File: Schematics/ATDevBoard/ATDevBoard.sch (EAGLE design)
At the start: 42 parts, among them U1 TINY85-20-DIP

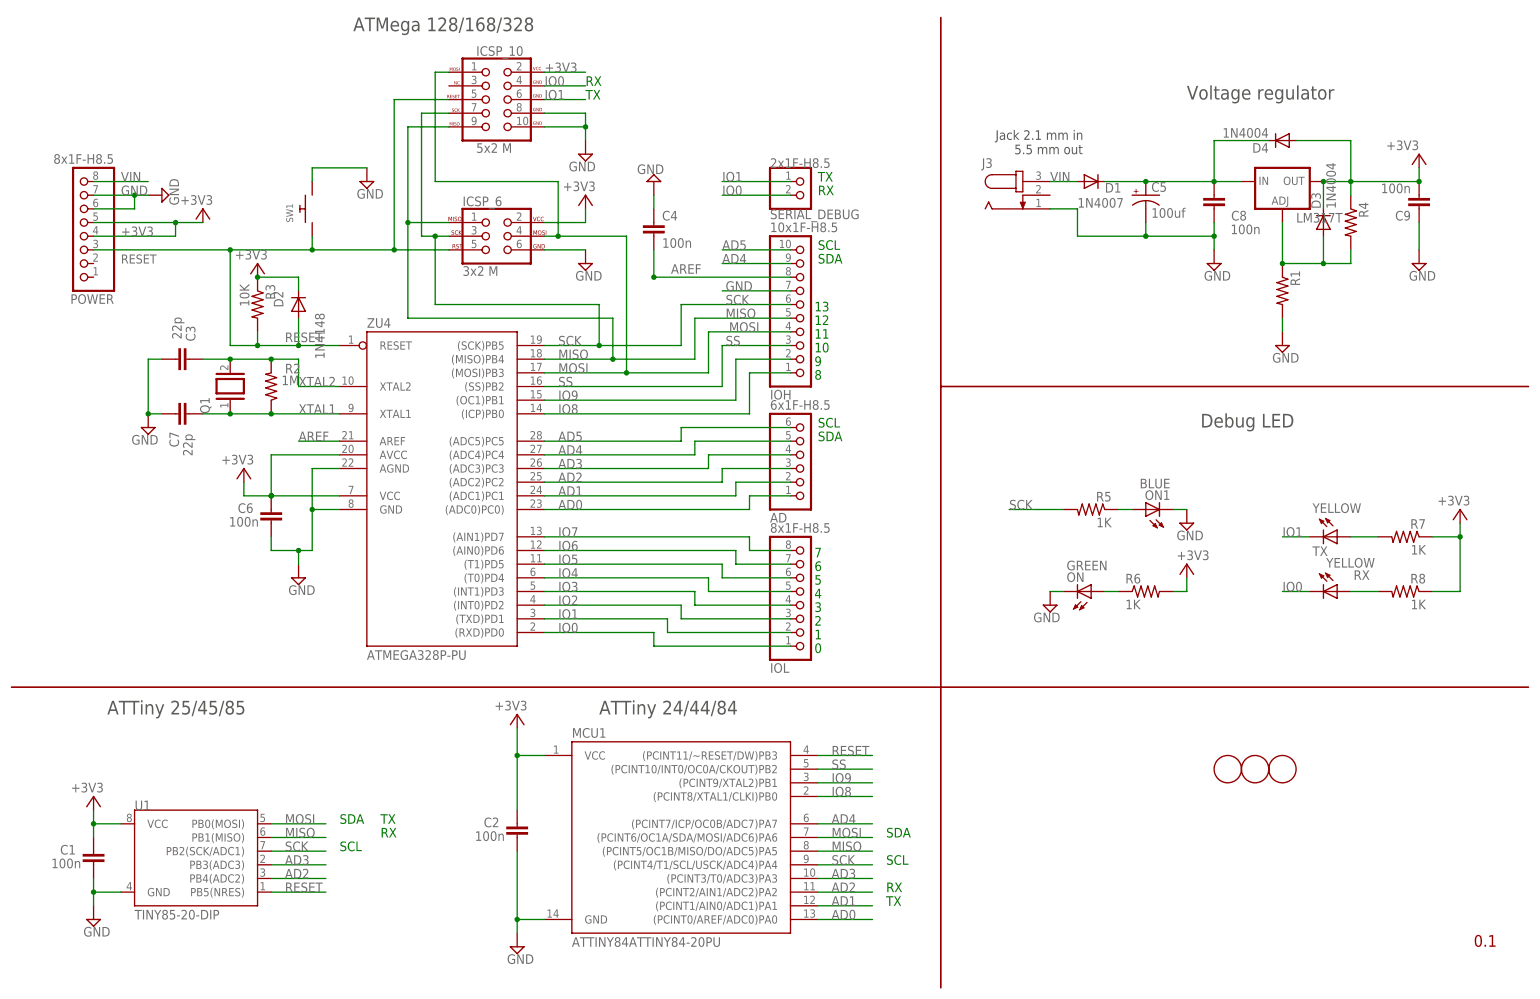
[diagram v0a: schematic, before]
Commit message: Added vaule for regulator resistors, first routed version of brd. Added pdfs for brd and schematic.
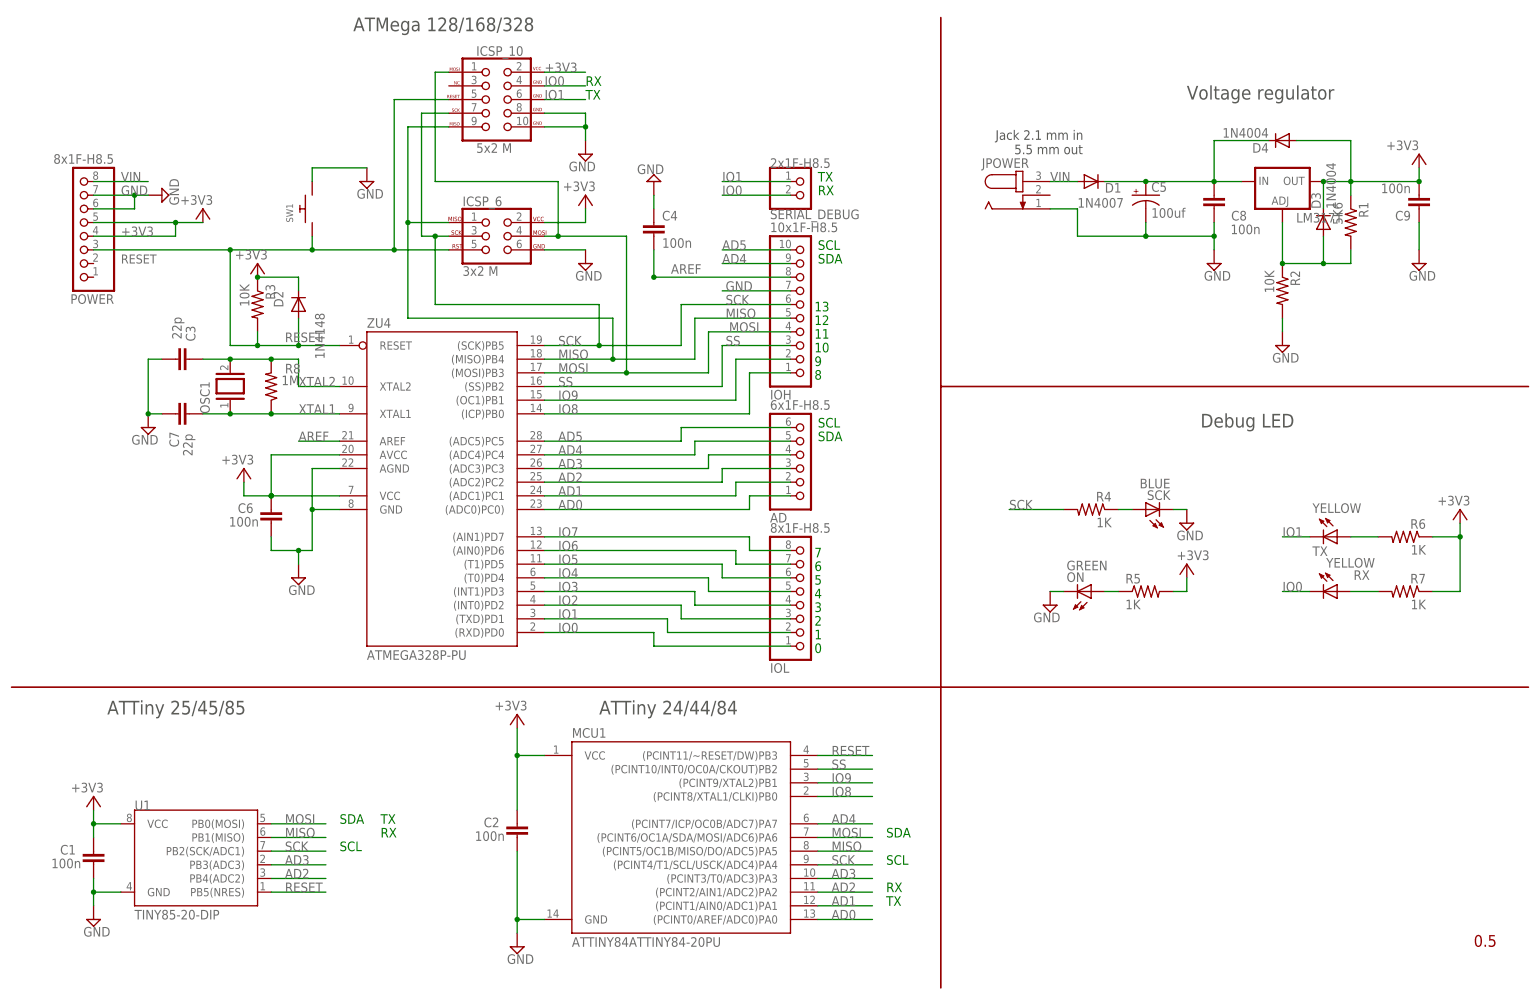
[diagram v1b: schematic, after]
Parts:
- removed FD1, FD2, FD3: FIDUCIALMOUNT, SmartPrj:FIDUCIALMOUNT
- R1: value (none) -> 5K6
- R2: value 1M -> 10K
- R4: value (none) -> 1K
- R8: value 1K -> 1M
- renumbered J3 to JPOWER, ON1 to SCK, Q1 to OSC1
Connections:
- net +3V3: now also R1.1, R5.2, R6.1; no longer R4.1, R6.2, R8.1
- net GND: now also R2.2; no longer R1.2
- net N$1: now also R1.2, R2.1; no longer R1.1, R4.2
- net N$3: now also R5.1; no longer R6.1
- net N$35: now also R7.2; no longer R8.2
- net N$36: now also R6.2; no longer R7.2
- net N$4: now also R4.1; no longer R5.1
- net SCK: now also R4.2; no longer R5.2
- net XTAL1: now also R8.1; no longer R2.1
- net XTAL2: now also R8.2; no longer R2.2
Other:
- moved on the sheet: R1, R2, R4, R5, R6, R7, R8

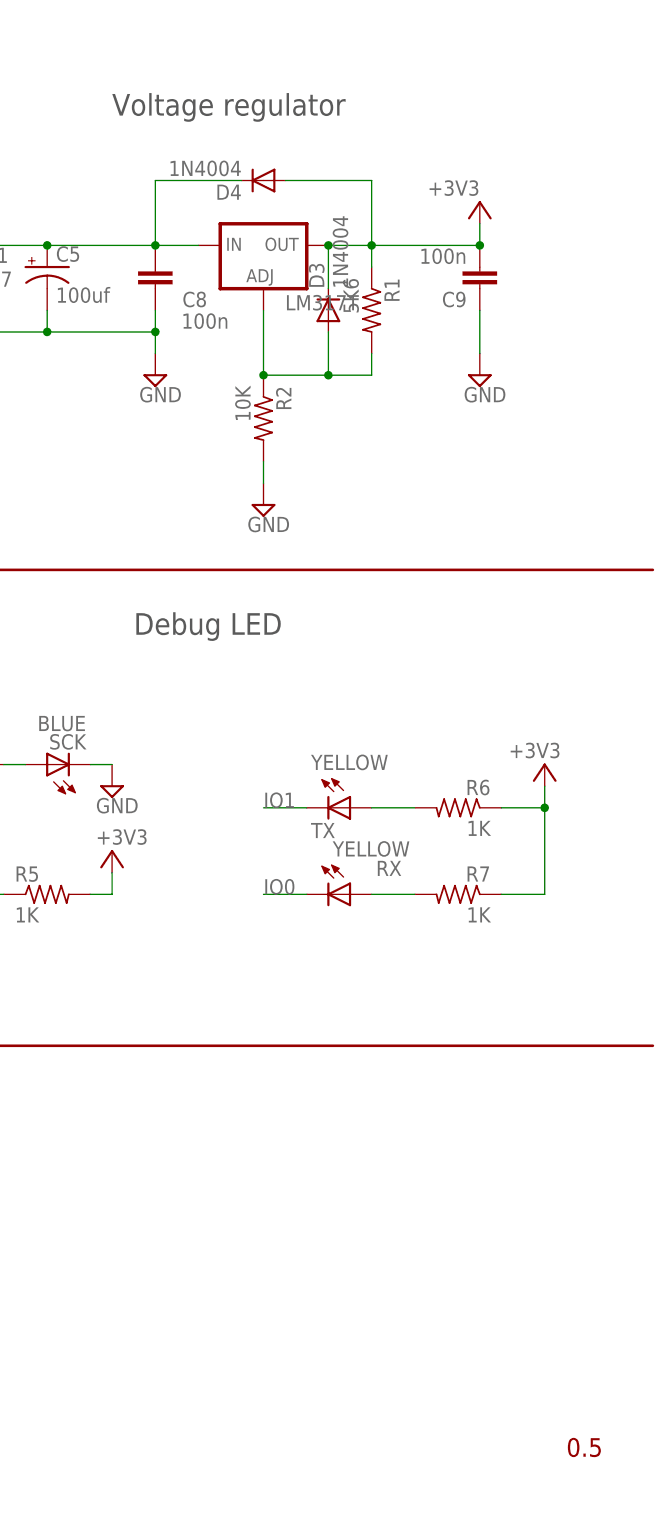
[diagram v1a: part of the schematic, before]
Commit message: Fixed packages for some resistors, replaced 1N4004 with 1N4007 diodes
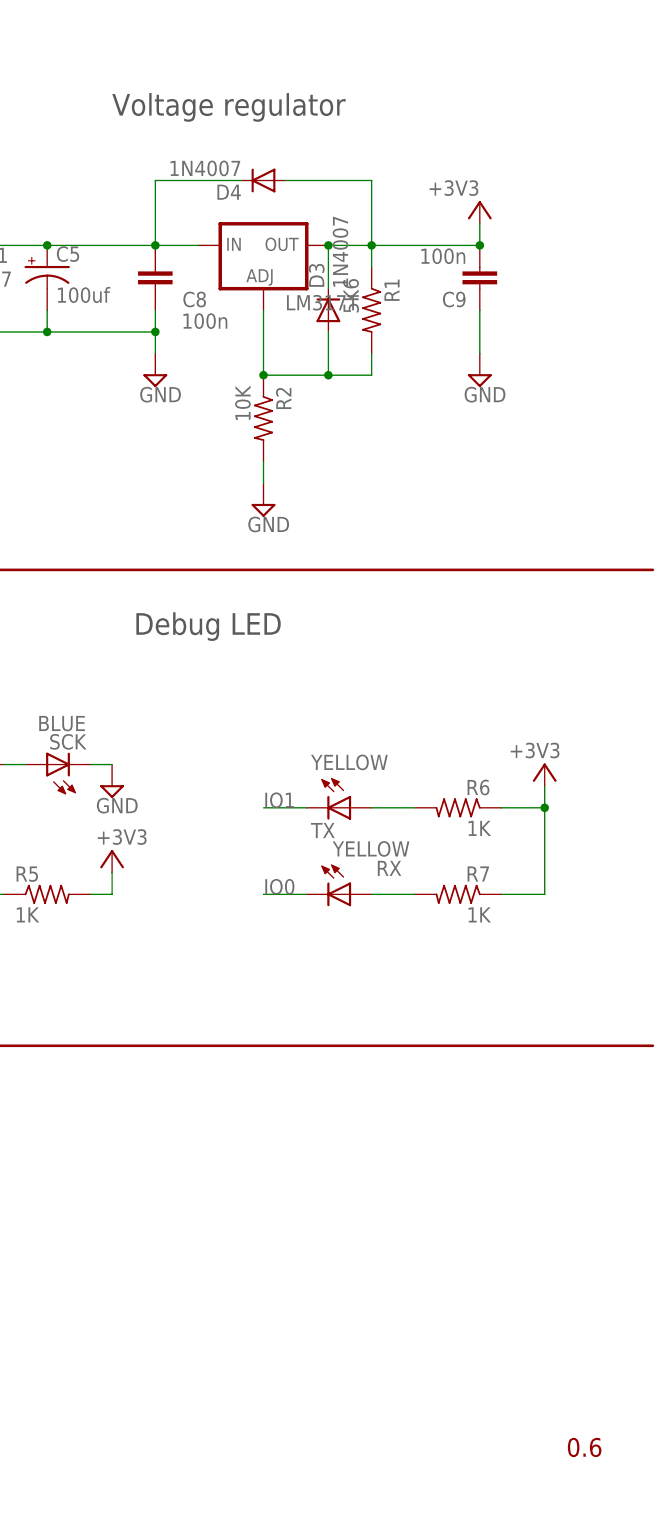
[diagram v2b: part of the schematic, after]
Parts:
- D3, D4: value 1N4004 -> 1N4007
- R4, R5, R6, R7: device rcl:R-US_0309/12 -> rcl:R-US_0207/10
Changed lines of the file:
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@@
 <grid distance="0.1" unitdist="inch" unit="inch" style="lines" multiple="1" display="no" altdistance="0.01" altunitdist="inch" altunit="inch"/>
 <layers>
-<layer number="1" name="Top" color="4" fill="1" visible="no" active="no"/>
-<layer number="16" name="Bottom" color="1" fill="1" visible="no" active="no"/>
-<layer number="17" name="Pads" color="2" fill="1" visible="no" active="no"/>
-<layer number="18" name="Vias" color="2" fill="1" visible="no" active="no"/>
-<layer number="19" name="Unrouted" color="6" fill="1" visible="no" active="no"/>
-<layer number="20" name="Dimension" color="15" fill="1" visible="no" active="no"/>
-<layer number="21" name="tPlace" color="7" fill="1" visible="no" active="no"/>
-<layer number="22" name="bPlace" color="7" fill="1" visible="no" active="no"/>
-<layer number="23" name="tOrigins" color="15" fill="1" visible="no" active="no"/>
-<layer number="24" name="bOrigins" color="15" fill="1" visible="no" active="no"/>
-<layer number="25" name="tNames" color="7" fill="1" visible="no" active="no"/>
-<layer number="26" name="bNames" color="7" fill="1" visible="no" active="no"/>
-<layer number="27" name="tValues" color="7" fill="1" visible="no" active="no"/>
-<layer number="28" name="bValues" color="7" fill="1" visible="no" active="no"/>
+<layer number="1" name="Top" color="4" fill="1" visible="yes" active="no"/>
+<layer number="16" name="Bottom" color="1" fill="1" visible="yes" active="no"/>
+<layer number="17" name="Pads" color="2" fill="1" visible="yes" active="no"/>
+<layer number="18" name="Vias" color="2" fill="1" visible="yes" active="no"/>
+<layer number="19" name="Unrouted" color="6" fill="1" visible="yes" active="no"/>
+<layer number="20" name="Dimension" color="15" fill="1" visible="yes" active="no"/>
+<layer number="21" name="tPlace" color="7" fill="1" visible="yes" active="no"/>
+<layer number="22" name="bPlace" color="7" fill="1" visible="yes" active="no"/>
+<layer number="23" name="tOrigins" color="15" fill="1" visible="yes" active="no"/>
+<layer number="24" name="bOrigins" color="15" fill="1" visible="yes" active="no"/>
+<layer number="25" name="tNames" color="7" fill="1" visible="yes" active="no"/>
+<layer number="26" name="bNames" color="7" fill="1" visible="yes" active="no"/>
+<layer number="27" name="tValues" color="7" fill="1" visible="yes" active="no"/>
+<layer number="28" name="bValues" color="7" fill="1" visible="yes" active="no"/>
 <layer number="29" name="tStop" color="7" fill="3" visible="no" active="no"/>
 <layer number="30" name="bStop" color="7" fill="6" visible="no" active="no"/>
@@
 <layer number="35" name="tGlue" color="7" fill="4" visible="no" active="no"/>
 <layer number="36" name="bGlue" color="7" fill="5" visible="no" active="no"/>
-<layer number="37" name="tTest" color="7" fill="1" visible="no" active="no"/>
-<layer number="38" name="bTest" color="7" fill="1" visible="no" active="no"/>
+<layer number="37" name="tTest" color="7" fill="1" visible="yes" active="no"/>
+<layer number="38" name="bTest" color="7" fill="1" visible="yes" active="no"/>
 <layer number="39" name="tKeepout" color="4" fill="11" visible="no" active="no"/>
 <layer number="40" name="bKeepout" color="1" fill="11" visible="no" active="no"/>
@@
 <layer number="44" name="Drills" color="7" fill="1" visible="no" active="no"/>
 <layer number="45" name="Holes" color="7" fill="1" visible="no" active="no"/>
-<layer number="46" name="Milling" color="3" fill="1" visible="no" active="no"/>
-<layer number="47" name="Measures" color="7" fill="1" visible="no" active="no"/>
-<layer number="48" name="Document" color="7" fill="1" visible="no" active="no"/>
-<layer number="49" name="Reference" color="7" fill="1" visible="no" active="no"/>
-<layer number="50" name="dxf" color="12" fill="1" visible="no" active="no"/>
-<layer number="51" name="tDocu" color="7" fill="1" visible="no" active="no"/>
-<layer number="52" name="bDocu" color="7" fill="1" visible="no" active="no"/>
-<layer number="53" name="tGND_GNDA" color="7" fill="1" visible="no" active="no"/>
-<layer number="54" name="bGND_GNDA" color="7" fill="1" visible="no" active="no"/>
-<layer number="56" name="wert" color="7" fill="1" visible="no" active="no"/>
-<layer number="57" name="tCAD" color="7" fill="1" visible="no" active="no"/>
-<layer number="59" name="tCarbon" color="7" fill="1" visible="no" active="no"/>
-<layer number="60" name="bCarbon" color="7" fill="1" visible="no" active="no"/>
+<layer number="46" name="Milling" color="3" fill="1" visible="yes" active="no"/>
+<layer number="47" name="Measures" color="7" fill="1" visible="yes" active="no"/>
+<layer number="48" name="Document" color="7" fill="1" visible="yes" active="no"/>
+<layer number="49" name="Reference" color="7" fill="1" visible="yes" active="no"/>
+<layer number="50" name="dxf" color="12" fill="1" visible="yes" active="no"/>
+<layer number="51" name="tDocu" color="7" fill="1" visible="yes" active="no"/>
+<layer number="52" name="bDocu" color="7" fill="1" visible="yes" active="no"/>
+<layer number="53" name="tGND_GNDA" color="7" fill="1" visible="yes" active="no"/>
+<layer number="54" name="bGND_GNDA" color="7" fill="1" visible="yes" active="no"/>
+<layer number="56" name="wert" color="7" fill="1" visible="yes" active="no"/>
+<layer number="57" name="tCAD" color="7" fill="1" visible="yes" active="no"/>
+<layer number="59" name="tCarbon" color="7" fill="1" visible="yes" active="no"/>
+<layer number="60" name="bCarbon" color="7" fill="1" visible="yes" active="no"/>
 <layer number="90" name="Modules" color="5" fill="1" visible="yes" active="yes"/>
 <layer number="91" name="Nets" color="2" fill="1" visible="yes" active="yes"/>
@@
 <schematic xreflabel="%F%N/%S" xrefpart="/%S.%C%R">
 <attributes>
-<attribute name="VERSION" value="0.5"/>
+<attribute name="VERSION" value="0.6"/>
 </attributes>
 <variantdefs>
@@
 <part name="R1" library="rcl" deviceset="R-US_" device="0309/12" value="5K6"/>
 <part name="R2" library="rcl" deviceset="R-US_" device="0309/12" value="10K"/>
-<part name="D3" library="diode" deviceset="1N4004" device=""/>
-<part name="D4" library="diode" deviceset="1N4004" device=""/>
+<part name="D3" library="diode" deviceset="1N4004" device="" value="1N4007"/>
+<part name="D4" library="diode" deviceset="1N4004" device="" value="1N4007"/>
 <part name="ICSP_10" library="SparkFun-Connectors" deviceset="AVR_SPI_PROG_5X2" device="PTH2" value="5x2 M"/>
 <part name="GND4" library="supply2" deviceset="GND" device=""/>
@@
 <part name="GND3" library="supply2" deviceset="GND" device=""/>
 <part name="R3" library="rcl" deviceset="R-US_" device="0309/12" value="10K"/>
-<part name="R4" library="rcl" deviceset="R-US_" device="0309/12" value="1K"/>
-<part name="R5" library="rcl" deviceset="R-US_" device="0309/12" value="1K"/>
-<part name="R6" library="rcl" deviceset="R-US_" device="0309/12" value="1K"/>
-<part name="R7" library="rcl" deviceset="R-US_" device="0309/12" value="1K"/>
+<part name="R4" library="rcl" deviceset="R-US_" device="0207/10" value="1K"/>
+<part name="R5" library="rcl" deviceset="R-US_" device="0207/10" value="1K"/>
+<part name="R6" library="rcl" deviceset="R-US_" device="0207/10" value="1K"/>
+<part name="R7" library="rcl" deviceset="R-US_" device="0207/10" value="1K"/>
 </parts>
 <sheets>
